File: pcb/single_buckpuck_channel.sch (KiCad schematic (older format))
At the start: 13 parts

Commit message: Finished schematic design, added new datasheets...
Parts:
- removed SW?: SPST, symbol SPST
- added P?: CONN_2, symbol CONN_2
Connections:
- wire segments 44 -> 49
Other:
- moved on the sheet: RV?

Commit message: Finished netlist, begun laying out board.  Added datasheets.
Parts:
- P5: renamed from P?; value CONN_2 -> CurrentOutput
- P6: renamed from P?; value CONN_2 -> OnOffSwitch
- gave numbers to parts that had none: 11

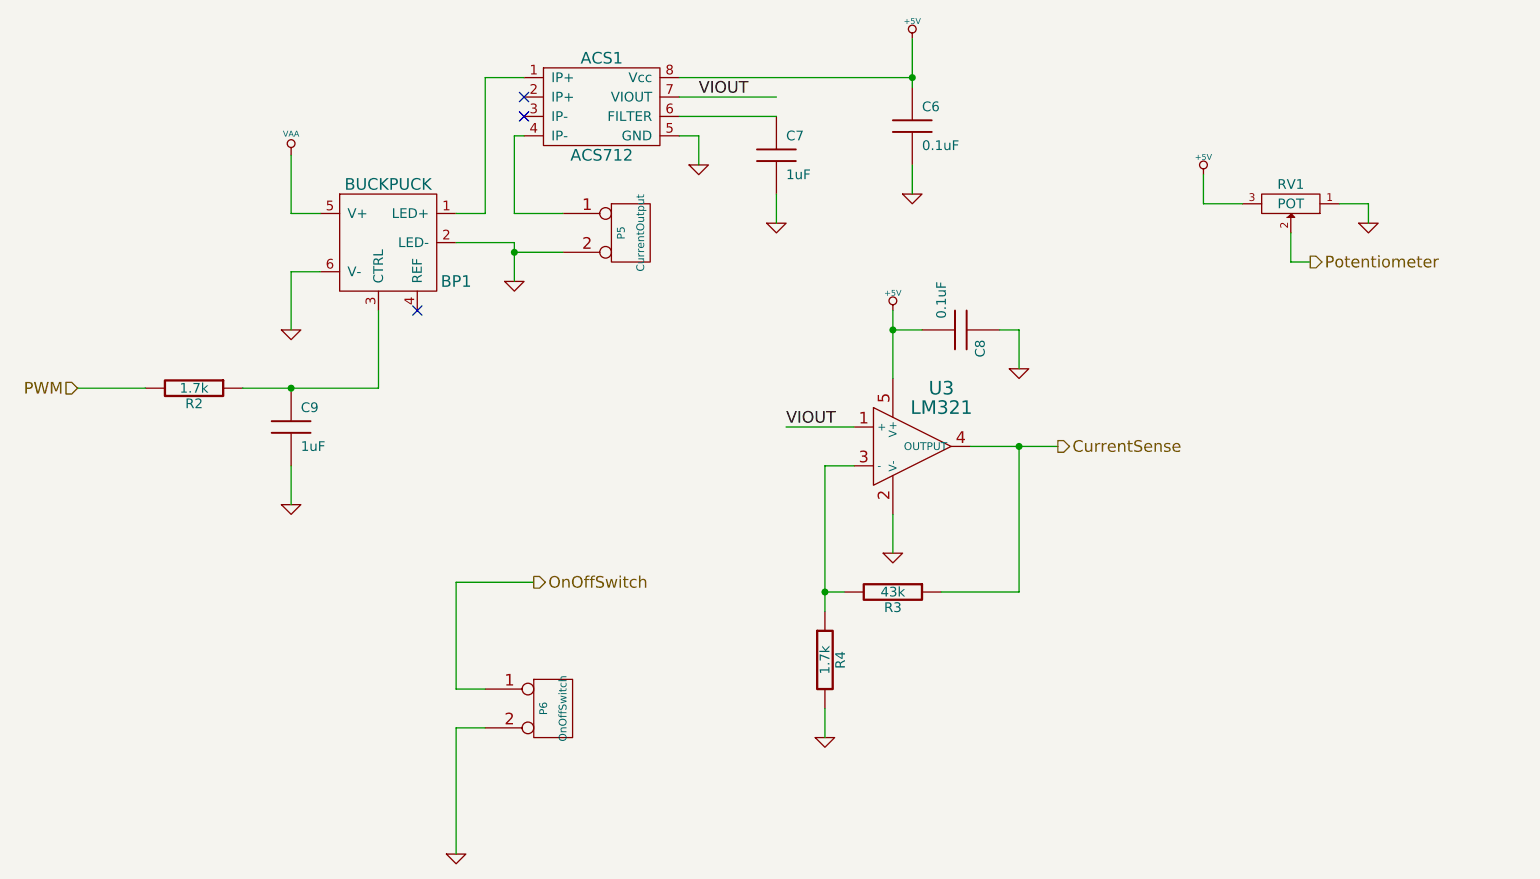
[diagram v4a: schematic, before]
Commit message: Modified schematic, board, and enclosure files
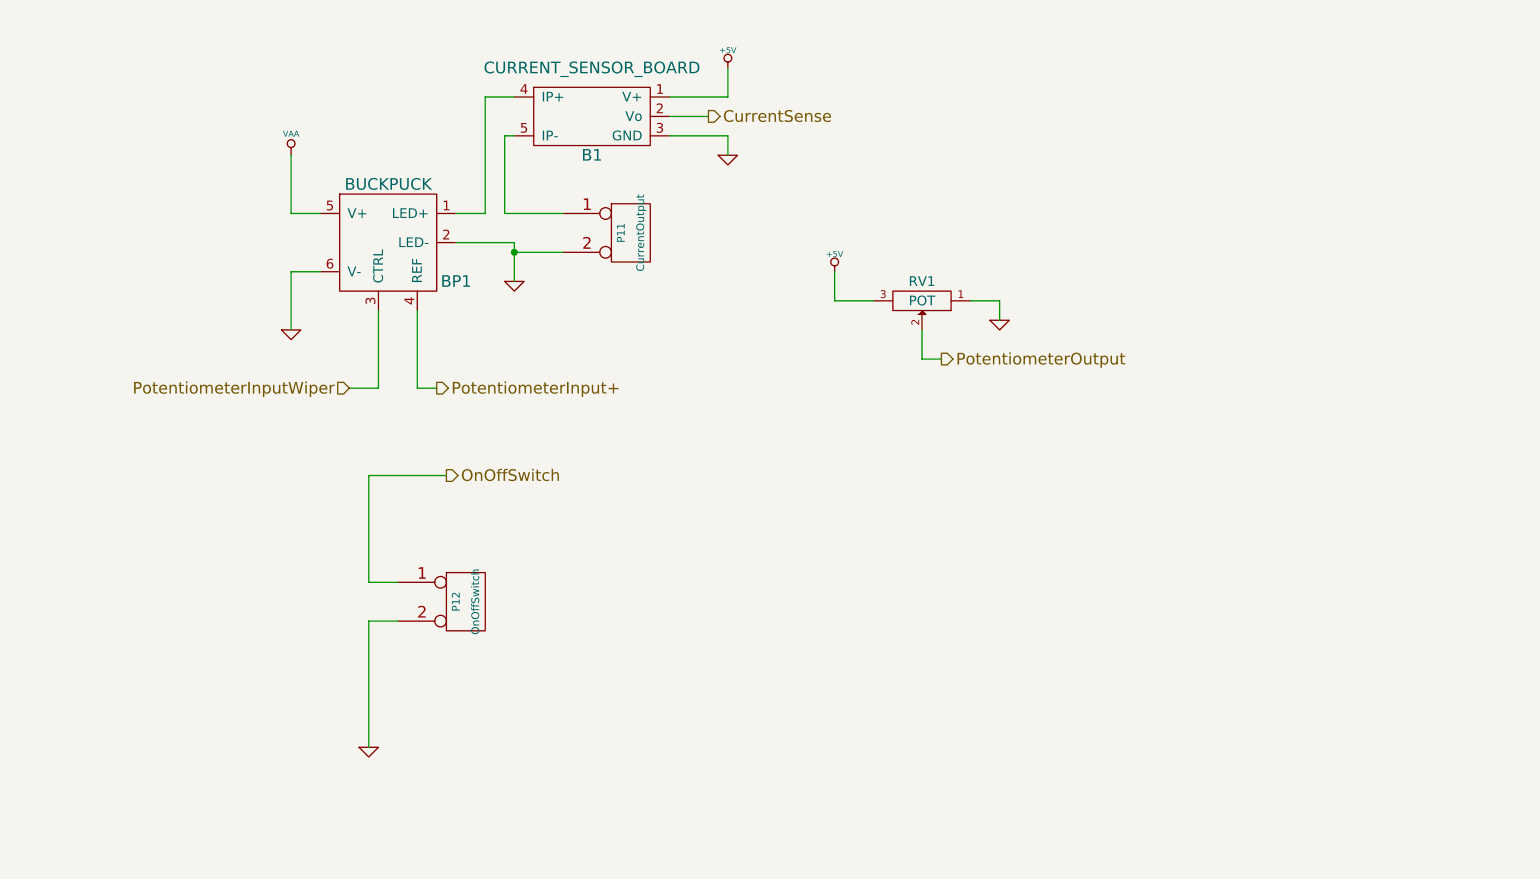
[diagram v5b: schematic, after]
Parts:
- removed ACS1: ACS712, symbol ACS712
- removed C6, C8: 0.1uF, symbol C
- removed C7, C9: 1uF, symbol C
- removed R2, R4: 1.7k, symbol R
- removed R3: 43k, symbol R
- removed U3: LM321, symbol LM321
- added B1: CURRENT_SENSOR_BOARD, symbol CURRENT_SENSOR_BOARD
- renumbered P5 to P11, P6 to P12
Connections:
- net +5V: now also B1.1 (V+)
- net CurrentSense: now also B1.2 (Vo)
- net GND: now also B1.3 (GND)
- net at P11.1 (P1): now also B1.5 (IP-)
- net at BP1.1 (LED+): now also B1.4 (IP+)
- net PotentiometerInputWiper: now reaches BP1.3 (CTRL)
- net PotentiometerInput+: now reaches BP1.4 (REF)
- net Potentiometer renamed PotentiometerOutput
- no-connect marks 3 -> 0
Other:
- moved on the sheet: P12, RV1
